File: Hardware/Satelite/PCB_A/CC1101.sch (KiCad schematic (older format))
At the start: 37 parts, among them U2 CC1101RGP, U3 0915BM15A0001E, U5 B39921B3588U410, U6 CC1190, Y1 26 MHz

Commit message: Completado nuevo PCB_A
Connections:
- net +3V3_Internal: now also U6.6 (HGM); no longer L5.1
- net GDO0: now also U6.7 (LNA_EN); no longer U6.8 (PA_EN)
- net GDO2: now also U6.8 (PA_EN); no longer U6.7 (LNA_EN)
- net VDD_PA: now also L5.1; no longer U6.6 (HGM)
- net at L2.1, U5.5 (OUT): now also C13.1
- net at L2.2, U6.10 (LNA_OUT), U6.11 (PA_IN): no longer C13.1
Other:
- moved on the sheet: C13, L2
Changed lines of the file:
@@
 Wire Wire Line
 	4500 2050 4500 1900
-Wire Wire Line
-	4450 1750 4650 1750
 $Comp
 L Device:C_Small C?
 U 1 1 5DCB1A77
-P 5100 2000
+P 4900 2000
 AR Path="/5B9997DB/5DCB1A77" Ref="C?"  Part="1"
 AR Path="/5B9A8077/5DCB1A77" Ref="C?"  Part="1"
 AR Path="/5BA17F9C/5DCB1A77" Ref="C13"  Part="1"
-F 0 "C13" H 5192 2046 50  0000 L CNN
-F 1 "0.8pF" H 5192 1955 50  0000 L CNN
-F 2 "Capacitor_SMD:C_0402_1005Metric" H 5100 2000 50  0001 C CNN
-F 3 "~" H 5100 2000 50  0001 C CNN
-F 4 "NP0" H 5100 2000 50  0001 C CNN "Dielectric"
-F 5 "GRM1555C2AR80BA01D" H 5100 2000 50  0001 C CNN "Manufacturer Part Number"
-	1    5100 2000
+F 0 "C13" H 4992 2046 50  0000 L CNN
+F 1 "0.8pF" H 4992 1955 50  0000 L CNN
+F 2 "Capacitor_SMD:C_0402_1005Metric" H 4900 2000 50  0001 C CNN
+F 3 "~" H 4900 2000 50  0001 C CNN
+F 4 "NP0" H 4900 2000 50  0001 C CNN "Dielectric"
+F 5 "GRM1555C2AR80BA01D" H 4900 2000 50  0001 C CNN "Manufacturer Part Number"
+	1    4900 2000
 	-1   0    0    -1
 $EndComp
@@
 L Device:L L?
 U 1 1 5DCB84D8
-P 4800 1750
+P 5200 1750
 AR Path="/5B9A8077/5DCB84D8" Ref="L?"  Part="1"
 AR Path="/5BA17F9C/5DCB84D8" Ref="L2"  Part="1"
-F 0 "L2" V 4900 1750 50  0000 L CNN
-F 1 "10nH" V 4750 1650 50  0000 L CNN
-F 2 "Inductor_SMD:L_0402_1005Metric" H 4800 1750 50  0001 C CNN
-F 3 "" H 4800 1750 50  0001 C CNN
-F 4 "LQG15HN10NH02D" V 4800 1750 50  0001 C CNN "Manufacturer Part Number"
-	1    4800 1750
+F 0 "L2" V 5300 1750 50  0000 L CNN
+F 1 "10nH" V 5150 1650 50  0000 L CNN
+F 2 "Inductor_SMD:L_0402_1005Metric" H 5200 1750 50  0001 C CNN
+F 3 "" H 5200 1750 50  0001 C CNN
+F 4 "LQG15HN10NH02D" V 5200 1750 50  0001 C CNN "Manufacturer Part Number"
+	1    5200 1750
 	0    -1   -1   0
 $EndComp
@@
 L power:GND #PWR?
 U 1 1 5DCBB81E
-P 5100 2200
+P 4900 2200
 AR Path="/5B9A8077/5DCBB81E" Ref="#PWR?"  Part="1"
 AR Path="/5BA17F9C/5DCBB81E" Ref="#PWR048"  Part="1"
-F 0 "#PWR048" H 5100 1950 50  0001 C CNN
-F 1 "GND" H 5105 2027 50  0000 C CNN
-F 2 "" H 5100 2200 50  0001 C CNN
-F 3 "" H 5100 2200 50  0001 C CNN
-	1    5100 2200
-	1    0    0    -1
-$EndComp
-Wire Wire Line
-	5100 2100 5100 2200
-Wire Wire Line
-	5100 1900 5100 1750
-Wire Wire Line
-	5100 1750 4950 1750
-Connection ~ 5100 1750
+F 0 "#PWR048" H 4900 1950 50  0001 C CNN
+F 1 "GND" H 4905 2027 50  0000 C CNN
+F 2 "" H 4900 2200 50  0001 C CNN
+F 3 "" H 4900 2200 50  0001 C CNN
+	1    4900 2200
+	1    0    0    -1
+$EndComp
+Wire Wire Line
+	4900 2100 4900 2200
+Wire Wire Line
+	4900 1900 4900 1750
 $Comp
 L Device:L L?
@@
 	7600 1750 7800 1750
 $Comp
-L AXTEC_IC:+3V3_Internal #PWR?
-U 1 1 5DCCF261
-P 7600 1250
-AR Path="/5DCCF261" Ref="#PWR?"  Part="1"
-AR Path="/5BA17F9C/5DCCF261" Ref="#PWR54"  Part="1"
-F 0 "#PWR54" H 7600 1650 50  0001 C CNN
-F 1 "+3V3_Internal" H 7585 1423 50  0000 C CNN
-F 2 "" H 7600 1250 50  0001 C CNN
-F 3 "" H 7600 1250 50  0001 C CNN
-	1    7600 1250
-	1    0    0    -1
-$EndComp
-Wire Wire Line
-	7600 1350 7600 1250
-$Comp
 L Device:L L?
 U 1 1 5DCDA4C3
@@
 Wire Wire Line
 	5800 1900 5600 1900
-Text Label 5350 2150 0    50   ~ 0
-VDD_PA
-Wire Wire Line
-	5100 1750 5600 1750
 Wire Wire Line
 	5600 1900 5600 1750
-Connection ~ 5600 1750
 Wire Wire Line
 	5600 1750 5800 1750
@@
 Wire Wire Line
 	5800 2500 5350 2500
+Text Label 5350 2500 0    50   ~ 0
+GDO2
 Text Label 5350 2400 0    50   ~ 0
-GDO2
-Text Label 5350 2500 0    50   ~ 0
 GDO0
 $Comp
@@
 	1    0    0    -1
 $EndComp
+Wire Wire Line
+	5350 1750 5600 1750
+Connection ~ 5600 1750
+Wire Wire Line
+	4450 1750 4900 1750
+Connection ~ 4900 1750
+Wire Wire Line
+	4900 1750 5050 1750
+Text Label 7200 1200 0    50   ~ 0
+VDD_PA
+Wire Wire Line
+	7600 1200 7200 1200
+Wire Wire Line
+	7600 1200 7600 1350
+$Comp
+L AXTEC_IC:+3V3_Internal #PWR?
+U 1 1 5E1A4DEA
+P 5350 2150
+AR Path="/5E1A4DEA" Ref="#PWR?"  Part="1"
+AR Path="/5BA17F9C/5E1A4DEA" Ref="#PWR54"  Part="1"
+F 0 "#PWR54" H 5350 2550 50  0001 C CNN
+F 1 "+3V3_Internal" H 5335 2323 50  0000 C CNN
+F 2 "" H 5350 2150 50  0001 C CNN
+F 3 "" H 5350 2150 50  0001 C CNN
+	1    5350 2150
+	1    0    0    -1
+$EndComp

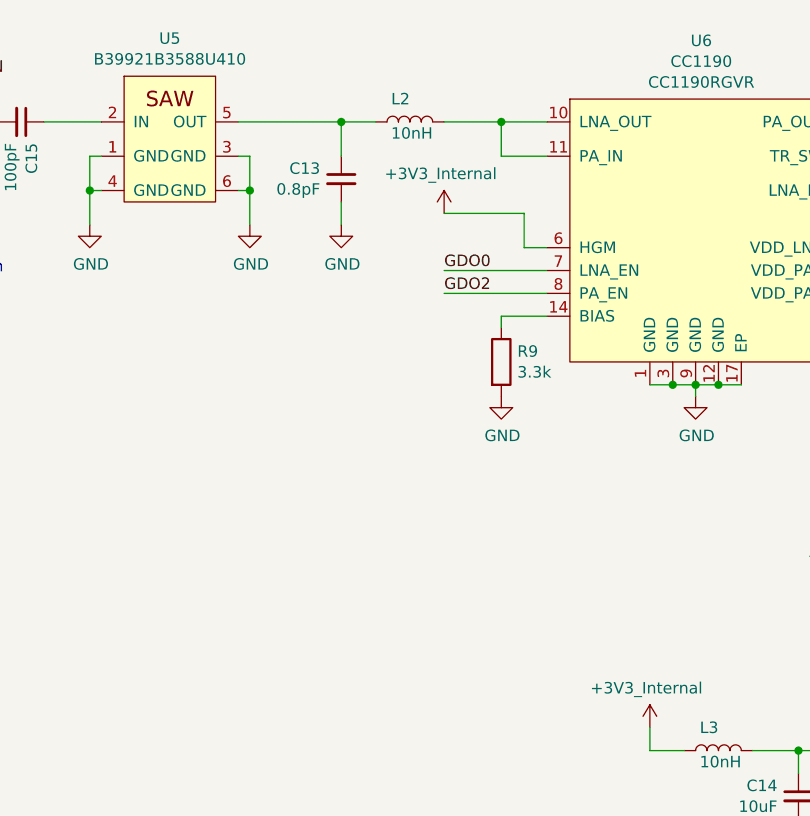
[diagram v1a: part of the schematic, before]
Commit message: Agregado jumper de seleción de ganacia para CC1190 en ET
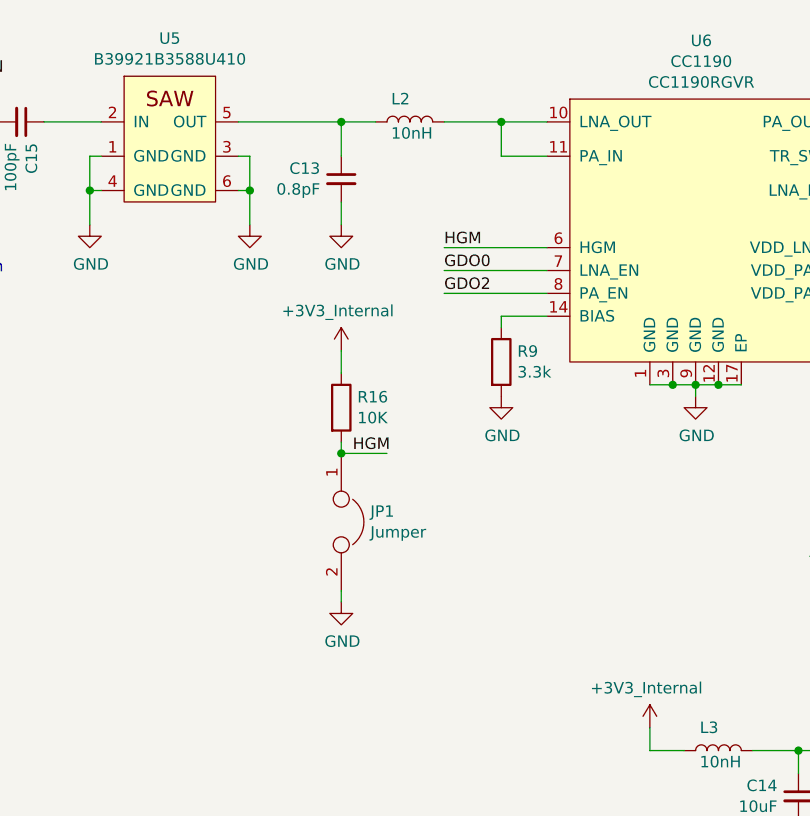
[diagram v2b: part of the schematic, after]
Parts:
- added JP1: Jumper, Jumper:SolderJumper-2_P1.3mm_Open_RoundedPad1.0x1.5mm, symbol Device:Jumper
- added R16: 10K, Resistor_SMD:R_0603_1608Metric_Pad1.05x0.95mm_HandSolder, symbol Device:R
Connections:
- net +3V3_Internal: now also R16.1; no longer U6.6 (HGM)
- net GND: now also JP1.2
- new net HGM: JP1.1, R16.2, U6.6 (HGM)
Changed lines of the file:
@@
 	5600 1750 5800 1750
-Wire Wire Line
-	5800 2300 5700 2300
-Wire Wire Line
-	5700 2300 5700 2150
-Wire Wire Line
-	5350 2150 5700 2150
 Wire Wire Line
 	5800 2400 5350 2400
@@
 L AXTEC_IC:+3V3_Internal #PWR?
 U 1 1 5E1A4DEA
-P 5350 2150
+P 4900 2750
 AR Path="/5E1A4DEA" Ref="#PWR?"  Part="1"
 AR Path="/5BA17F9C/5E1A4DEA" Ref="#PWR54"  Part="1"
-F 0 "#PWR54" H 5350 2550 50  0001 C CNN
-F 1 "+3V3_Internal" H 5335 2323 50  0000 C CNN
-F 2 "" H 5350 2150 50  0001 C CNN
-F 3 "" H 5350 2150 50  0001 C CNN
-	1    5350 2150
-	1    0    0    -1
-$EndComp
+F 0 "#PWR54" H 4900 3150 50  0001 C CNN
+F 1 "+3V3_Internal" H 4885 2923 50  0000 C CNN
+F 2 "" H 4900 2750 50  0001 C CNN
+F 3 "" H 4900 2750 50  0001 C CNN
+	1    4900 2750
+	1    0    0    -1
+$EndComp
+$Comp
+L power:GND #PWR?
+U 1 1 5CD45ACE
+P 4900 3850
+AR Path="/5B9A8077/5CD45ACE" Ref="#PWR?"  Part="1"
+AR Path="/5BA17F9C/5CD45ACE" Ref="#PWR059"  Part="1"
+F 0 "#PWR059" H 4900 3600 50  0001 C CNN
+F 1 "GND" H 4905 3677 50  0000 C CNN
+F 2 "" H 4900 3850 50  0001 C CNN
+F 3 "" H 4900 3850 50  0001 C CNN
+	1    4900 3850
+	1    0    0    -1
+$EndComp
+$Comp
+L Device:R R?
+U 1 1 5CD45AD5
+P 4900 3000
+AR Path="/5B9A8077/5CD45AD5" Ref="R?"  Part="1"
+AR Path="/5BA17F9C/5CD45AD5" Ref="R16"  Part="1"
+F 0 "R16" H 4970 3046 50  0000 L CNN
+F 1 "10K" H 4970 2955 50  0000 L CNN
+F 2 "Resistor_SMD:R_0603_1608Metric_Pad1.05x0.95mm_HandSolder" V 4830 3000 50  0001 C CNN
+F 3 "~" H 4900 3000 50  0001 C CNN
+F 4 "RC0603JR-0710KL" H 4900 3000 50  0001 C CNN "Manufacturer Part Number"
+	1    4900 3000
+	1    0    0    -1
+$EndComp
+Text Label 4950 3200 0    50   ~ 0
+HGM
+Wire Wire Line
+	4900 2750 4900 2850
+$Comp
+L Device:Jumper JP?
+U 1 1 5CD45AE3
+P 4900 3500
+AR Path="/5B9A8077/5CD45AE3" Ref="JP?"  Part="1"
+AR Path="/5BA17F9C/5CD45AE3" Ref="JP1"  Part="1"
+F 0 "JP1" V 4854 3627 50  0000 L CNN
+F 1 "Jumper" V 4945 3627 50  0000 L CNN
+F 2 "Jumper:SolderJumper-2_P1.3mm_Open_RoundedPad1.0x1.5mm" H 4900 3500 50  0001 C CNN
+F 3 "~" H 4900 3500 50  0001 C CNN
+	1    4900 3500
+	0    1    1    0
+$EndComp
+Wire Wire Line
+	4900 3150 4900 3200
+Wire Wire Line
+	4900 3800 4900 3850
+Wire Wire Line
+	4900 3200 5100 3200
+Connection ~ 4900 3200
+Text Label 5350 2300 0    50   ~ 0
+HGM
+Wire Wire Line
+	5350 2300 5800 2300
 $EndSCHEMATC

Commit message: PCB_A BOM
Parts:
- U6: Manufactuer Part Number CC1190RGVR -> (none); Manufacturer Part Number (none) -> CC1190RGVR
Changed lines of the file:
@@
 F 2 "Package_DFN_QFN:Texas_S-PVQFN-N16_EP2.7x2.7mm" H 6450 2250 50  0001 C CNN
 F 3 "" H 6300 1800 50  0001 C CNN
-F 4 "CC1190RGVR" H 6475 2023 50  0000 C CNN "Manufactuer Part Number"
+F 4 "CC1190RGVR" H 6475 2023 50  0000 C CNN "Manufacturer Part Number"
 	1    6300 1800
 	1    0    0    -1
